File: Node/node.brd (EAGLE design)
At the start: 160 x 100 mm, 64 parts, among them J1 U.FL, SW1 SWITCH-MOMENTARY-2PTH, SW2 SWITCH-MOMENTARY-2PTH, SW3 SWITCH-MOMENTARY-2PTH, U2 DW1000-I, U4 ATMEGA328, X2 332-02, Y1 8MHz

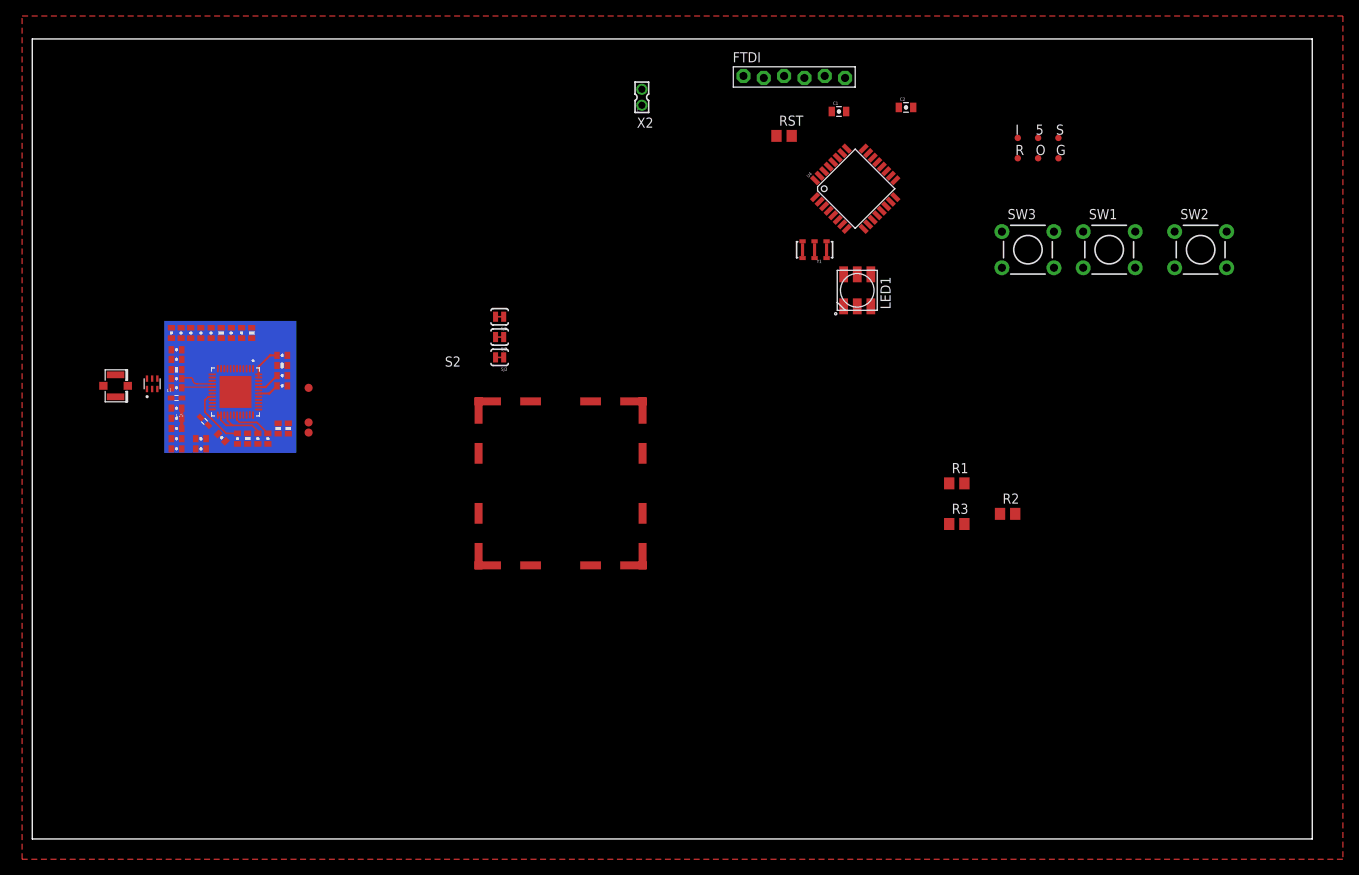
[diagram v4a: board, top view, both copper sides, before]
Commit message: Added the RF Shield to the sch and brd, then routed all components of the current schematic
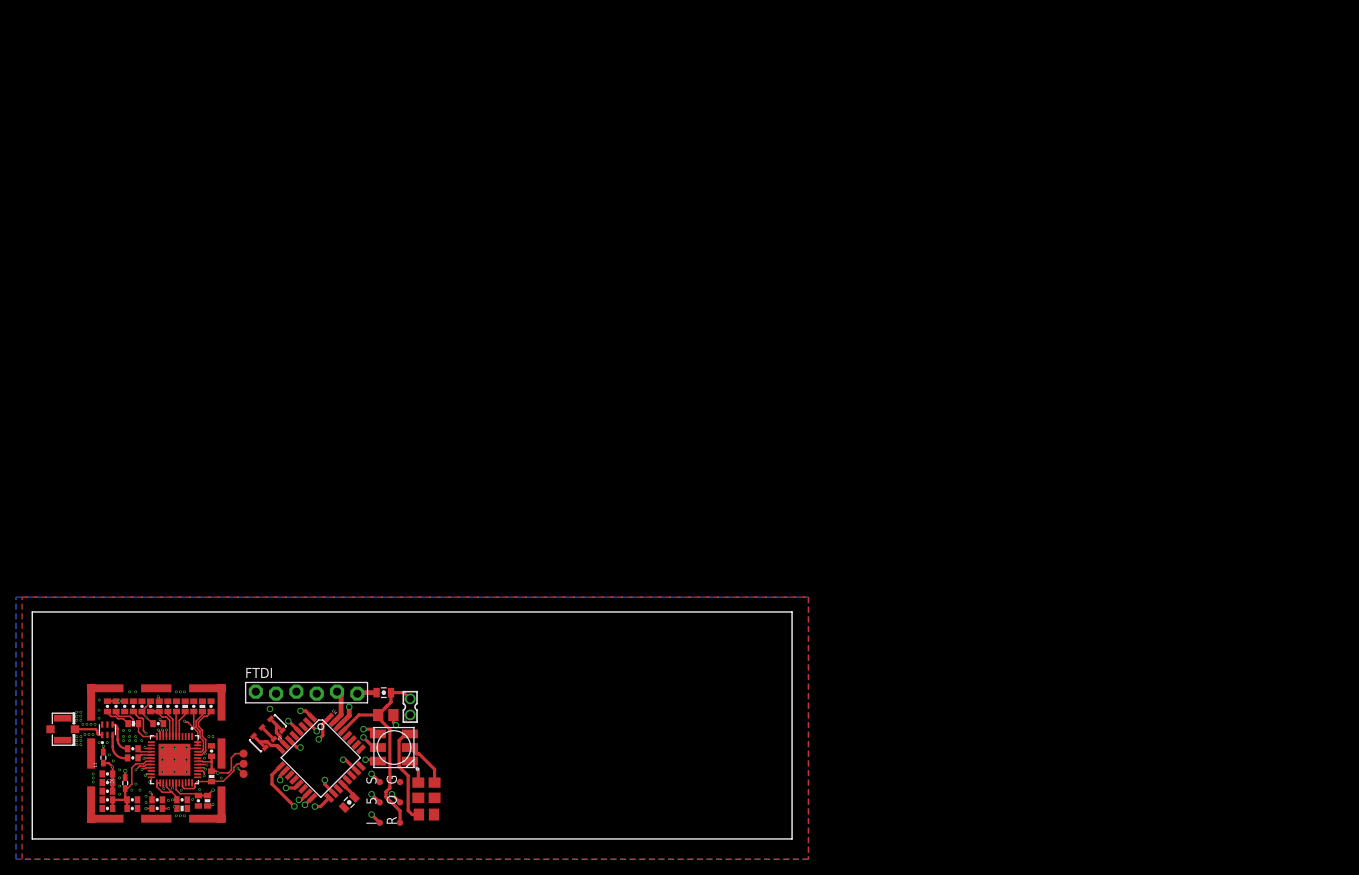
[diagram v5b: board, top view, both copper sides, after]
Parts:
- removed S2: WE-SHC_36103205, Wurth_Elektronik_Passive_rev15e:WE-SHC_36103205
- removed SJ1, SJ2, SJ3: SOLDERJUMPERTRACE, SparkFun-Retired:SJ_2S-TRACE
- removed SW1, SW2, SW3: SWITCH-MOMENTARY-2PTH, SparkFun-Electromechanical:TACTILE-PTH
- added U$1: 5BMI-S-202-F, MainLib:BMI-S-102
- moved I 117.0 mm to (43.4, 2.03), turned to 90 degrees
- moved S 117.0 mm to (43.4, 7.11), turned to 90 degrees
- moved 5 116.9 mm to (43.4, 4.57), turned to 90 degrees
- moved R 113.4 mm to (46.0, 2.03), turned to 90 degrees
- moved G 113.4 mm to (46.0, 7.11), turned to 90 degrees
- moved O 113.3 mm to (46.0, 4.57), turned to 90 degrees
- moved C2 111.3 mm to (39.6, 4.57), turned to 225 degrees
- moved FTDI 98.2 mm to (34.3, 18.3)
- moved U4 97.6 mm to (36.1, 10.2), turned to 315 degrees
- moved C1 92.3 mm to (43.9, 18.3)
- moved Y1 91.2 mm to (29.5, 13.2), turned to 225 degrees
- moved RST 87.9 mm to (44.2, 15.5)
- moved R2 81.8 mm to (49.3, 3.05), turned to 180 degrees
- moved X2 81.5 mm to (47.2, 16.5)
- moved LED1 81.4 mm to (45.2, 11.4), turned to 0 degrees
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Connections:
- net BAL_3 renamed BAL_N
- net BAL_4 renamed BAL_P
- removed net D2: SW2.3
- removed net SPICLK: SJ1.2, U2.41
- removed net SPIMISO: SJ2.2, U2.40
- removed net SPIMOSI: SJ3.2, U2.39
- net A3: no longer SW1.3
- net D10: no longer SW3.3
- net GND: now also U$1.P$1, U$1.P$10, U$1.P$11, U$1.P$12, U$1.P$2, U$1.P$3, U$1.P$4, U$1.P$5, U$1.P$6, U$1.P$7, U$1.P$8, U$1.P$9; no longer S2.1, SW1.1, SW2.1, SW3.1
- net MISO: now also U2.40; no longer SJ2.1
- net MOSI: now also U2.39; no longer SJ3.1
- net SCK: now also U2.41; no longer SJ1.1
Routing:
- net MOSI: track 0.00 -> 39.6 mm, vias 0 -> 3
- net EXTON: track 0.00 -> 34.5 mm, vias 0 -> 2
- net !SPICS: track 0.00 -> 32.3 mm, vias 0 -> 2
- net MISO: track 0.00 -> 31.7 mm, vias 0 -> 3
- net SCK: track 0.00 -> 31.5 mm, vias 0 -> 3
- net GRN: track 0.00 -> 30.1 mm, vias 0 -> 3
- net WAKEUP: track 0.00 -> 29.8 mm, vias 0 -> 3
- net !RST: track 0.00 -> 29.1 mm, vias 0 -> 2
- net RED: track 0.00 -> 27.2 mm, vias 0 -> 2
- net RESET: track 0.00 -> 26.8 mm
- net GPIO6: track 0.00 -> 14.8 mm, vias 0 -> 3
- net BLU: track 0.00 -> 14.1 mm, vias 0 -> 2
- net N$3: track 0.00 -> 13.3 mm
- net N$10: track 10.7 -> 23.9 mm, vias 0 -> 3
- net 3.3V: track 12.3 -> 23.9 mm, vias 0 -> 11
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- added copper zone on layer 15, net 3.3V
- added copper zone on layer 16, net GND
- added copper zone on layer 2, net GND
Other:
- board size 160 x 100 mm -> 95 x 28.4 mm

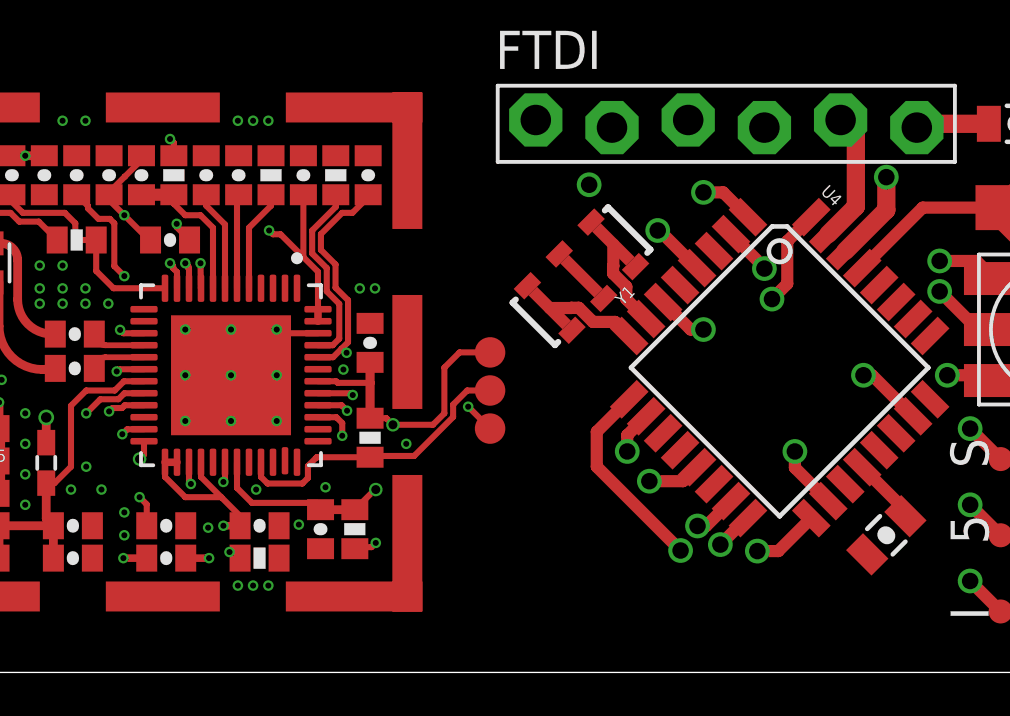
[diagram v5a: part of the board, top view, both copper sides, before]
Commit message: Added IRQ to an ATMEGA Int pin, isolated !RST behind a solder bubble
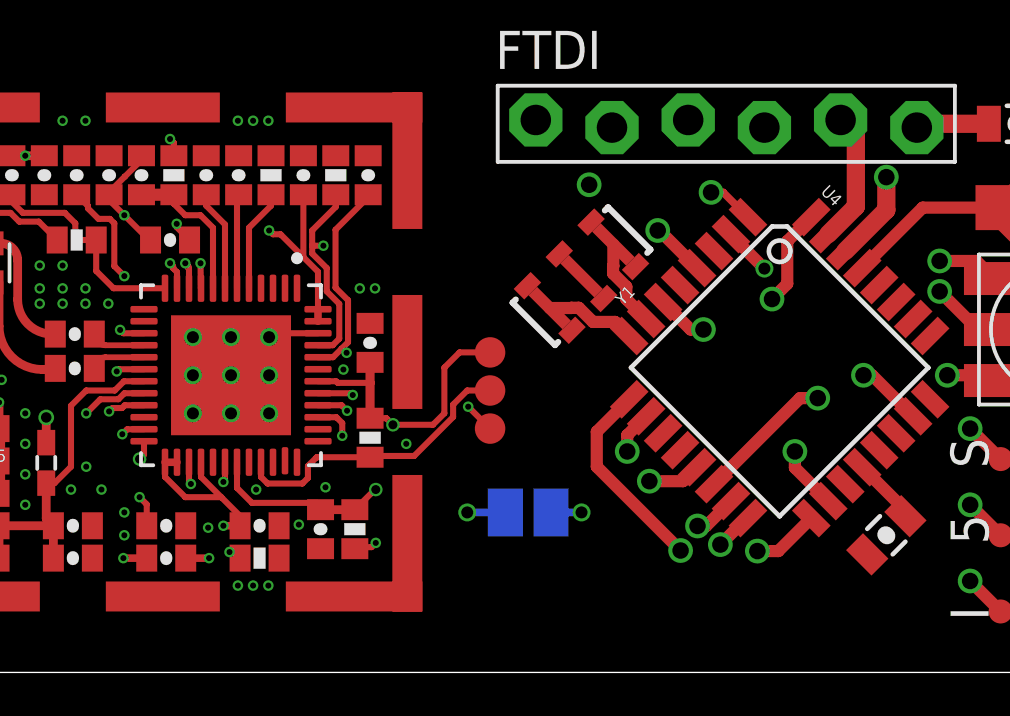
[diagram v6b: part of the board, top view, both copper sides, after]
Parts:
- added SJ1: (no value), jumper:SJ
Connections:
- removed net D10: U4.14
- removed net N$16: R7.2, U2.45
- new net D4: SJ1.1, U4.2
- new net IQR: R7.2, U2.45, U4.1
- net !RST: now also SJ1.2; no longer U4.2
- net BLU: now also U4.14; no longer U4.1
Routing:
- net IQR: track 0.00 -> 26.4 mm, vias 0 -> 2
- net !RST: track 29.1 -> 13.1 mm
- net D4: track 0.00 -> 14.5 mm, vias 0 -> 2
- net N$16: track 6.30 -> 0.00 mm
- net BLU: track 14.1 -> 10.9 mm
- net N$10: track 23.9 -> 23.3 mm

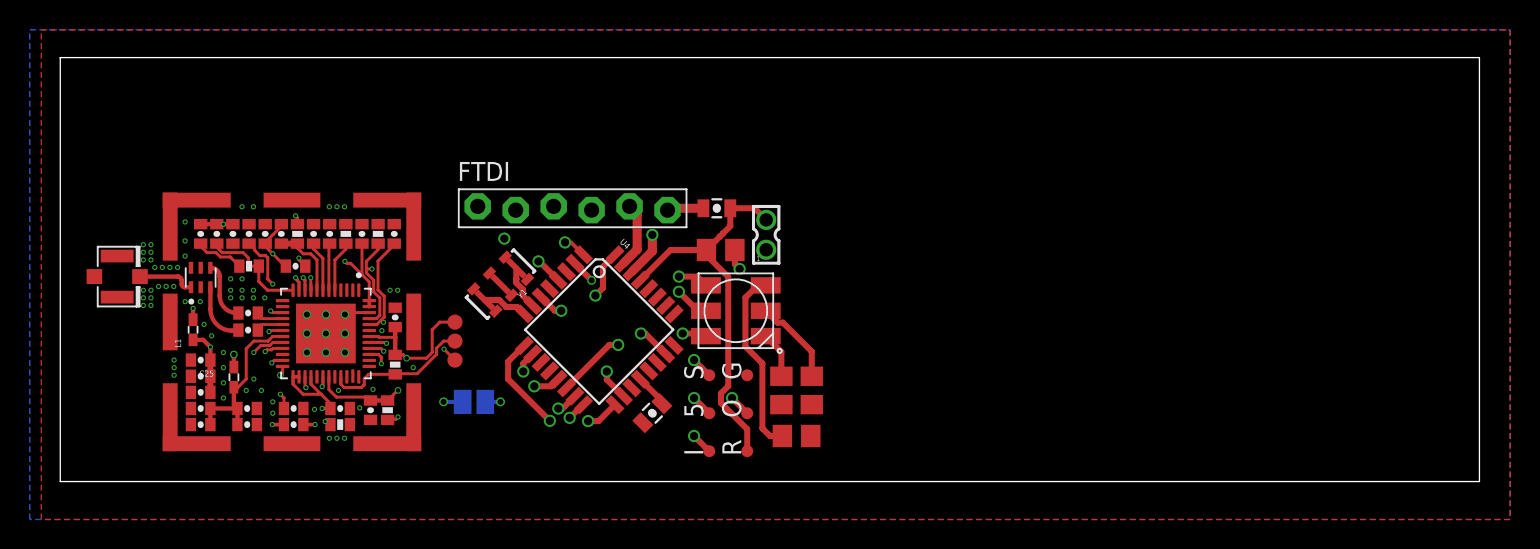
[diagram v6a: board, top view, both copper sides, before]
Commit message: Added TX and RX leds for the DW1000
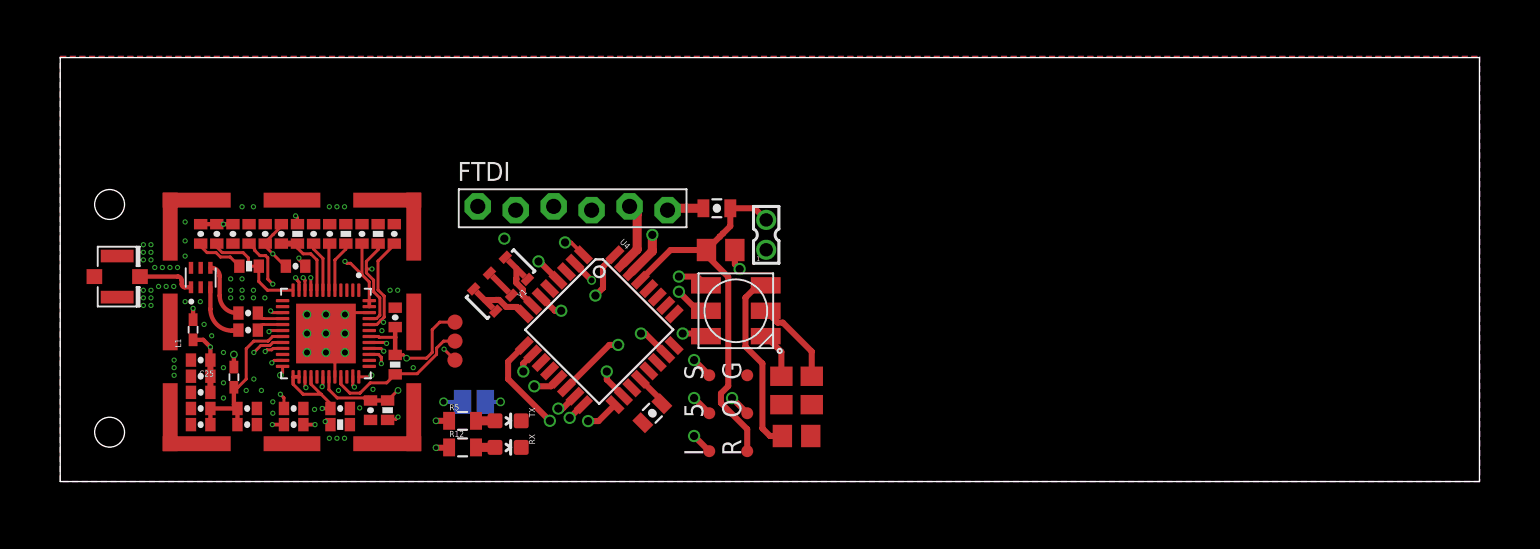
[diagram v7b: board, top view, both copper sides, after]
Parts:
- added R12, R5: 470, SparkFun-Passives:0805
- added RX, TX: (no value), SparkFun-LED:LED-0603
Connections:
- new net N$5: R5.2, TX.A
- new net N$6: R12.2, RX.A
- net GND: now also RX.C, TX.C
- net GPIO2: now also R12.1
- net GPIO3: now also R5.1
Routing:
- net GPIO3: track 0.00 -> 12.4 mm, vias 0 -> 2
- net GPIO2: track 0.00 -> 9.90 mm, vias 0 -> 2
- net GND: track 2.46 -> 4.37 mm
- net N$6: track 0.00 -> 1.27 mm
- net N$5: track 0.00 -> 1.27 mm

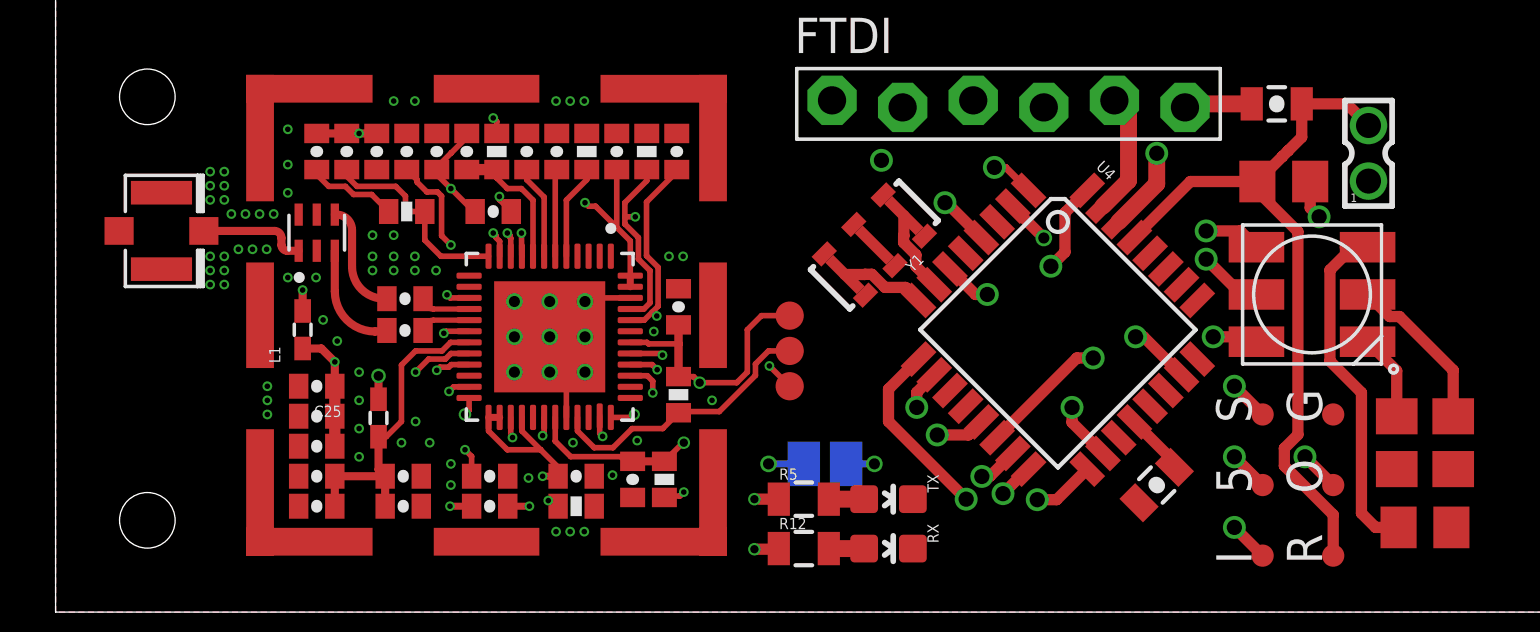
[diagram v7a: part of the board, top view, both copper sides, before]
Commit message: Moved the antenna such that the impedance lines are parallel and straight. Also added internal ground plane isolation for the buried antenna wire
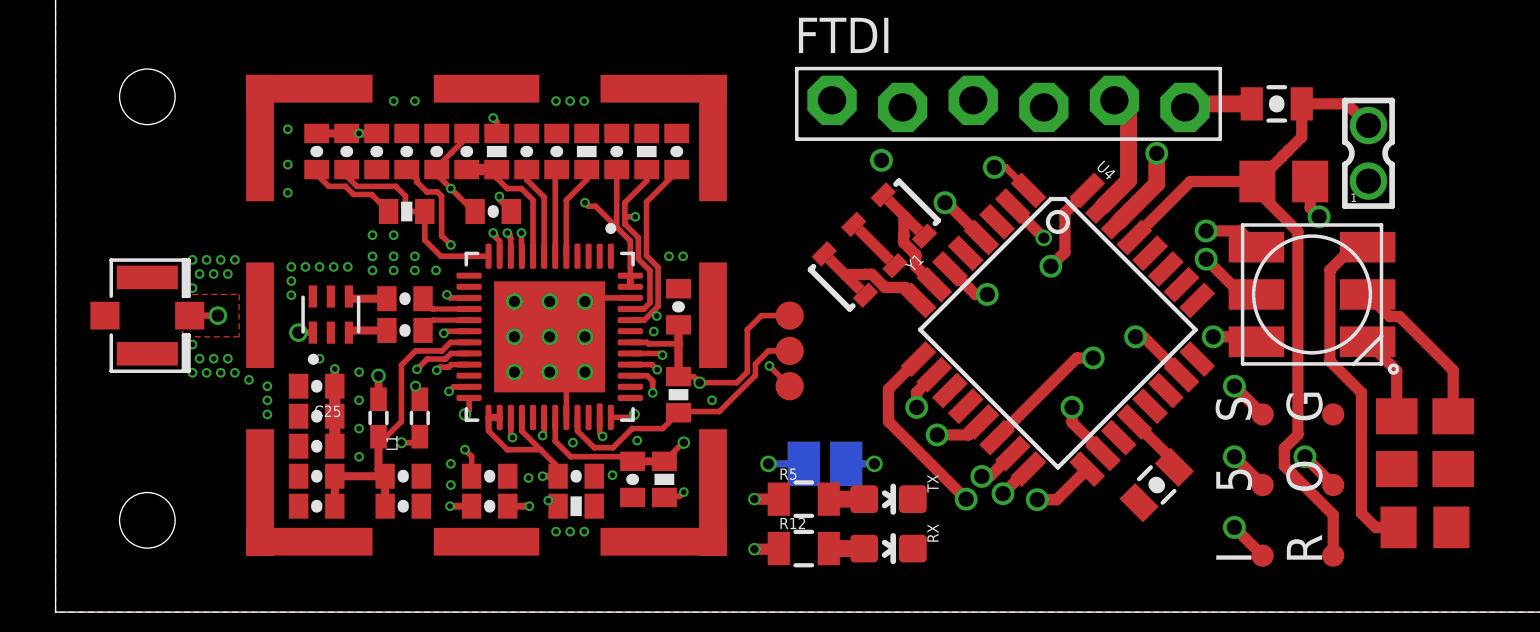
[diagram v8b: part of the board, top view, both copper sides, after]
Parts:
- moved L1 5.28 mm to (13.1, 6.99)
- moved J1 3.09 mm to (3.30, 10.7)
- moved BALUN1 2.99 mm to (9.91, 10.7)
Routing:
- net BAL_N: track 3.94 -> 1.40 mm
- net BAL_P: track 3.90 -> 1.40 mm
- net VDDPA1: track 9.90 -> 12.2 mm, vias 2 -> 3
- net ANT: track 3.86 -> 4.68 mm, vias 0 -> 2
- net N$3: track 13.3 -> 12.5 mm
- net RESET: track 26.8 -> 26.1 mm
- net GND: vias 73 -> 72
- added copper zone on layer 1, net ANT
- added copper zone on layer 15, net ANT
- added copper zone on layer 15, net GND
